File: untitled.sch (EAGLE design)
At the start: 70 parts, among them IC1 SIM900, IC2 ST1S10PHR, IC3 SMF05C, IC5 BQ24072, IC6 SIM68R, X1 ST-SMB-H, X2 ST-SMB-H

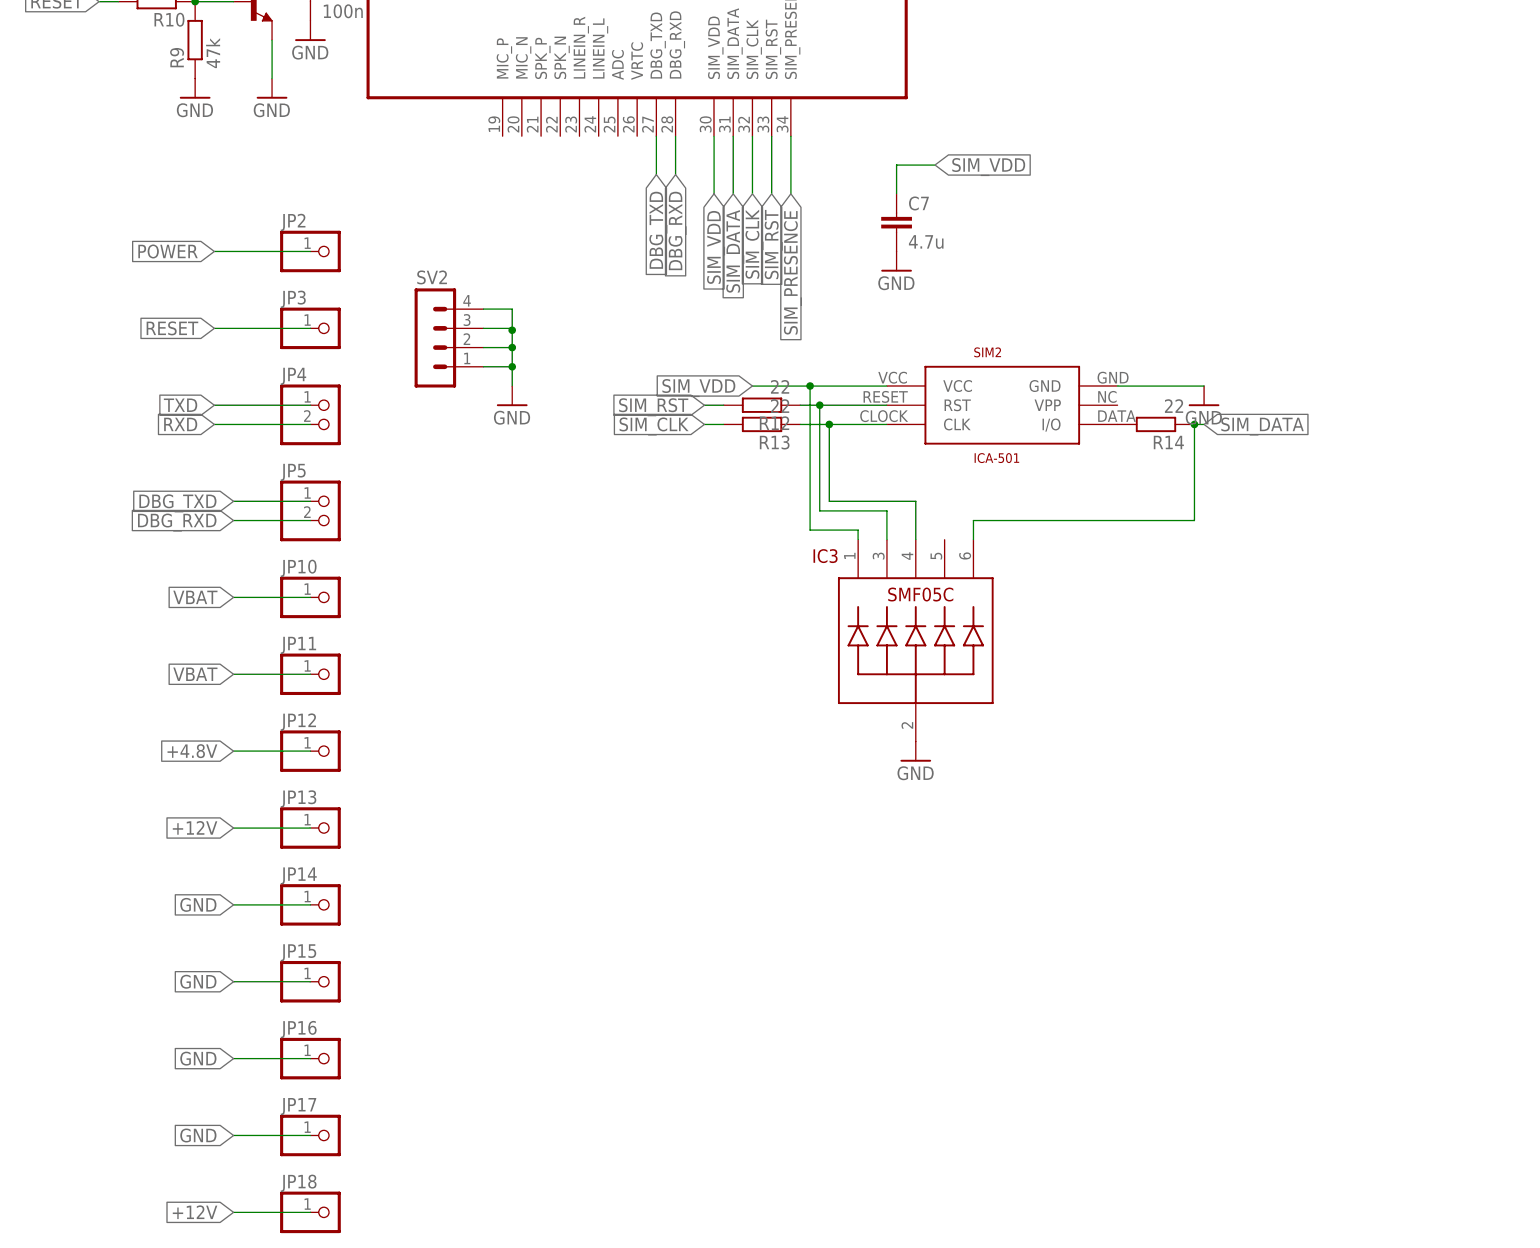
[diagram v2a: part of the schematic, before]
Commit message: SeedStudio preparation
GSM fotprint, polygons, thermals
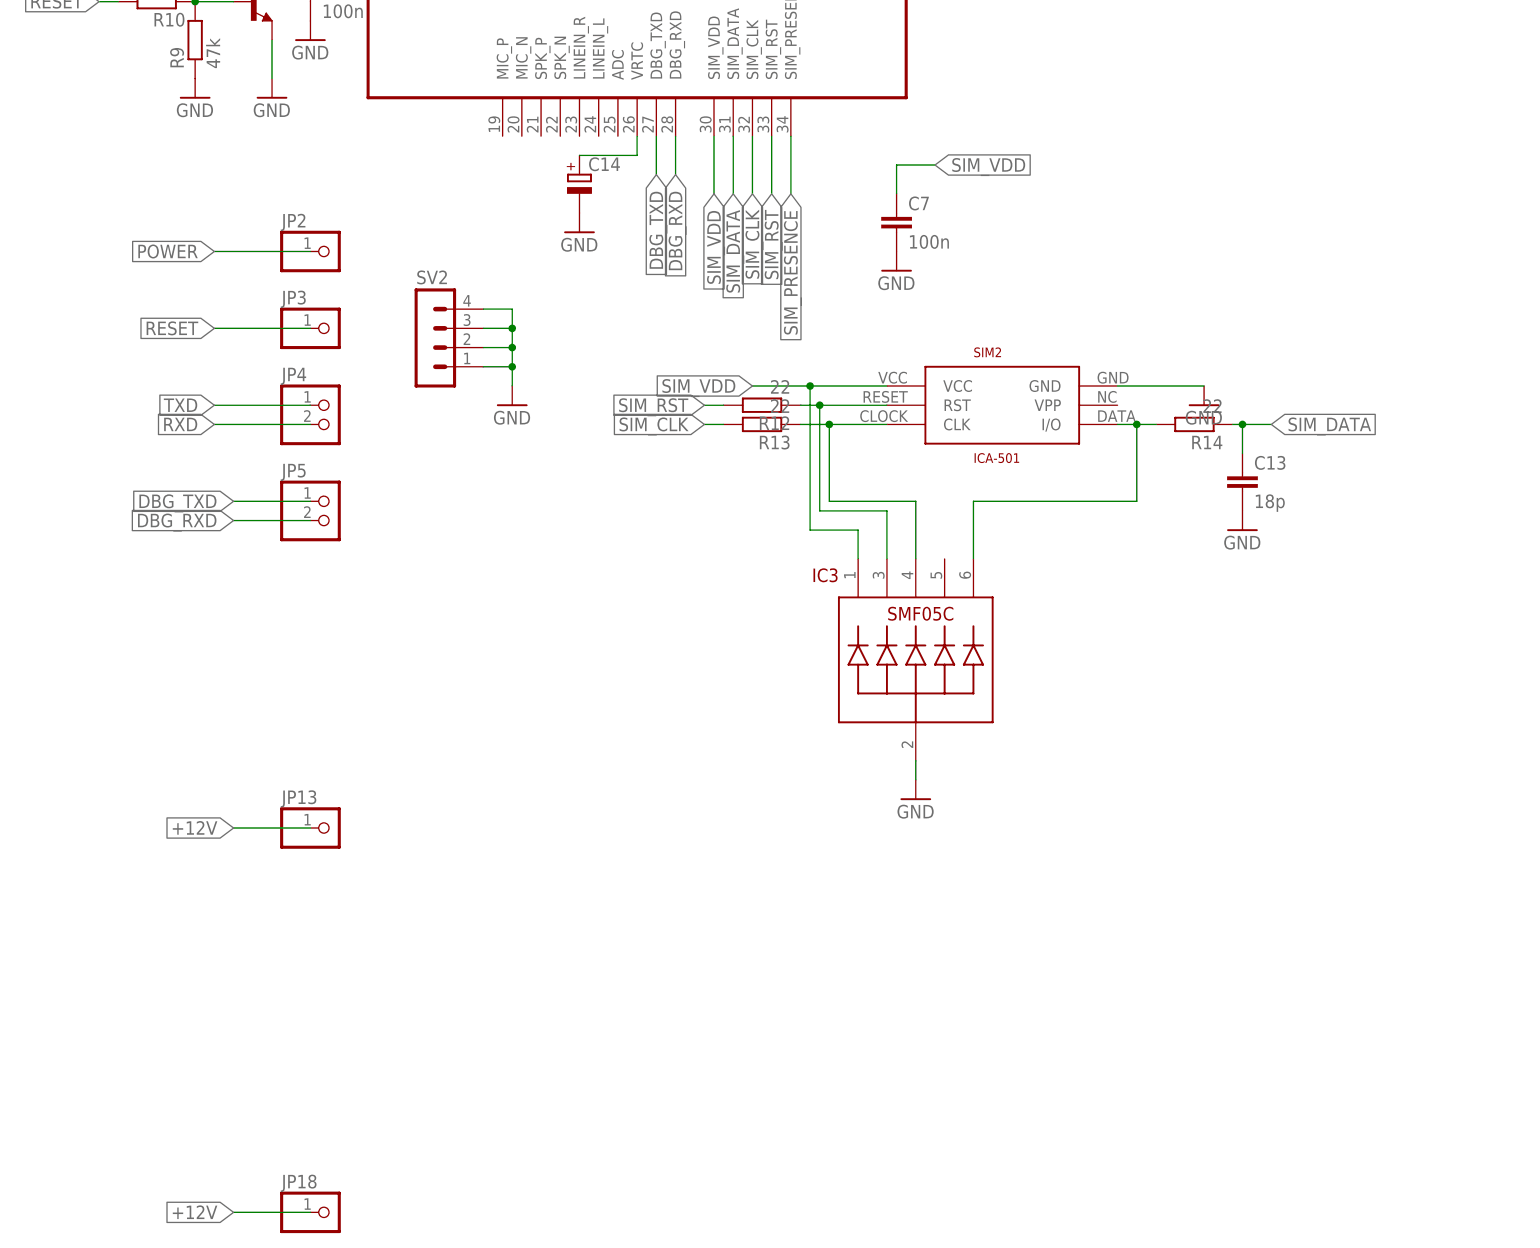
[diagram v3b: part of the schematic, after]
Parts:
- removed JP10, JP11, JP12, JP14, JP15, JP16, JP17: (no value), pinhead:PINHD-1X1
- added C13: 18p, resistor:C-EUC0805
- added C14: (no value), rcl:CPOL-EUA/3216-18R
- C7: value 4.7u -> 100n
- L1: device CDRH6D38:INDUCTOR-SUMIDA-CDRH4D18 -> inductor-sumida-cdrh4d18:INDUCTOR-SUMIDA-CDRH4D18
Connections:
- new net N$15: IC3.6, R14.2, SIM2.I/O
- net +4.8V: no longer JP12.1
- net GND: now also C13.2, C14.-; no longer JP14.1, JP15.1, JP16.1, JP17.1
- net N$17: now also C14.+, IC1G$1.VRTC; no longer R14.2, SIM2.I/O
- net SIM_DATA: now also C13.1; no longer IC3.6
- net VBAT: no longer JP10.1, JP11.1
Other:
- moved on the sheet: IC3, R14

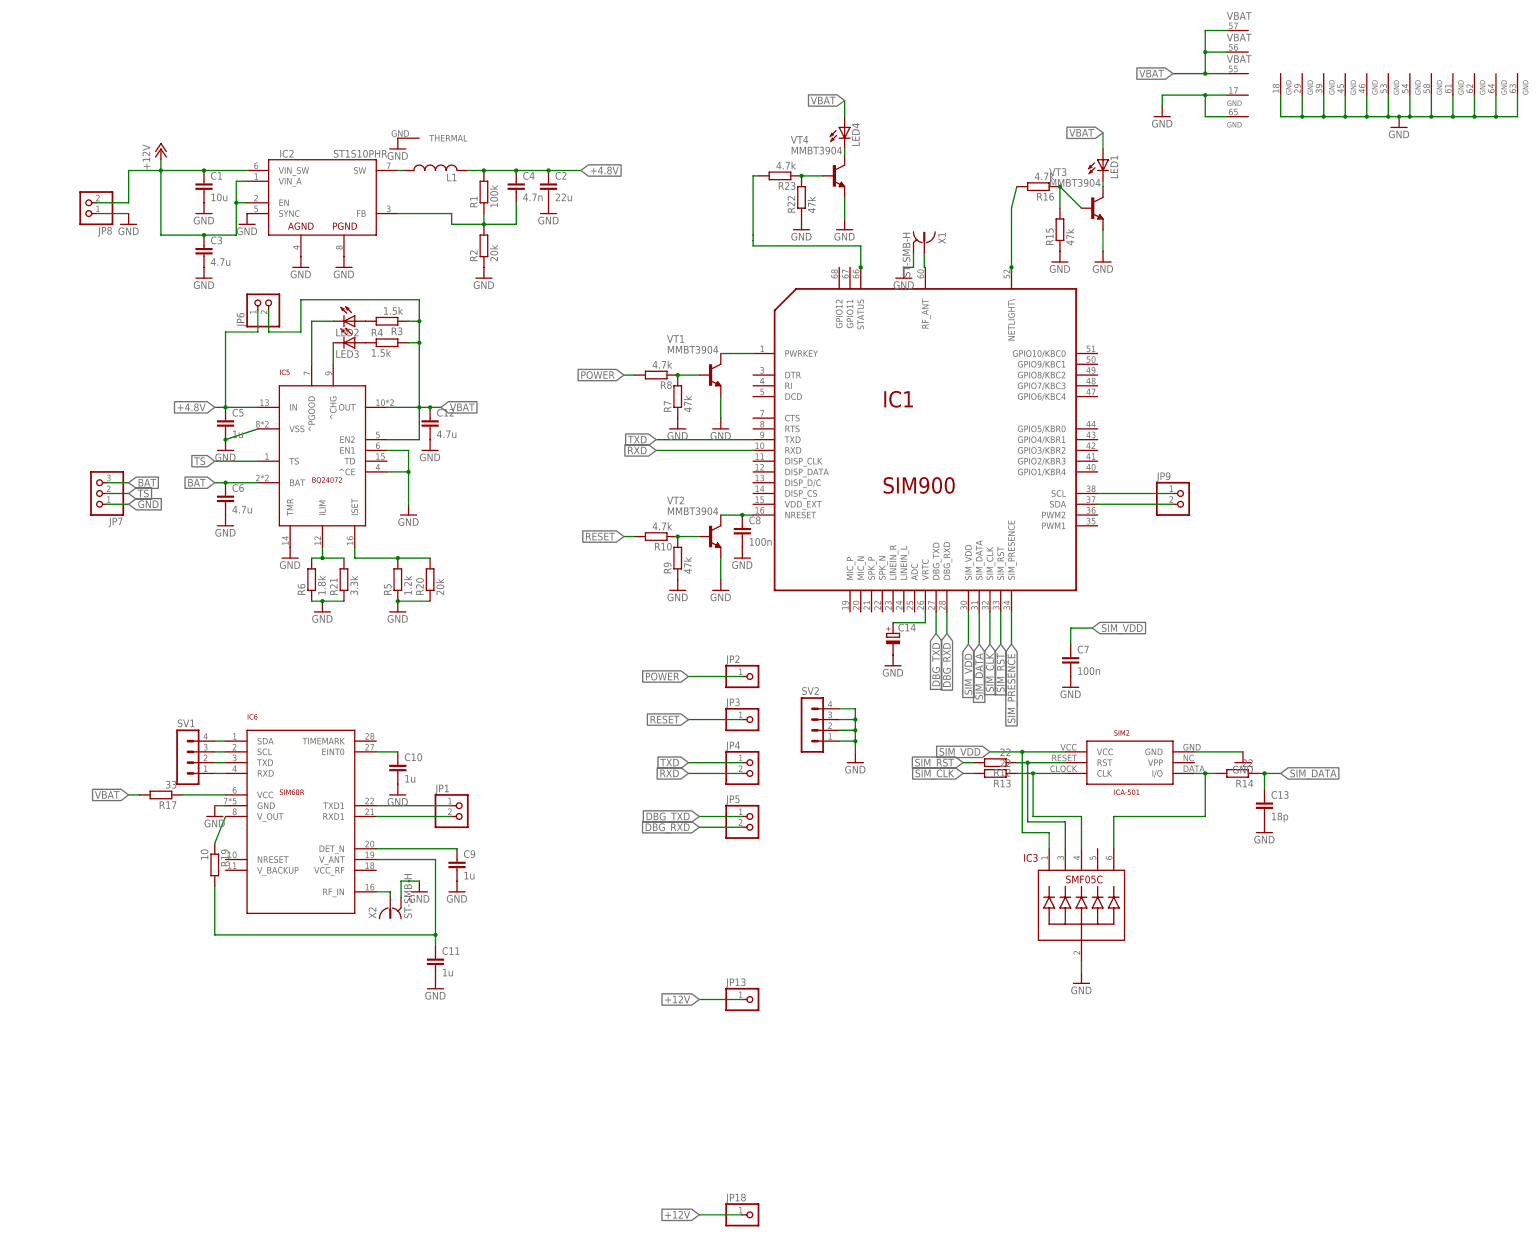
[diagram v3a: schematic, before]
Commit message: BQ now on the top
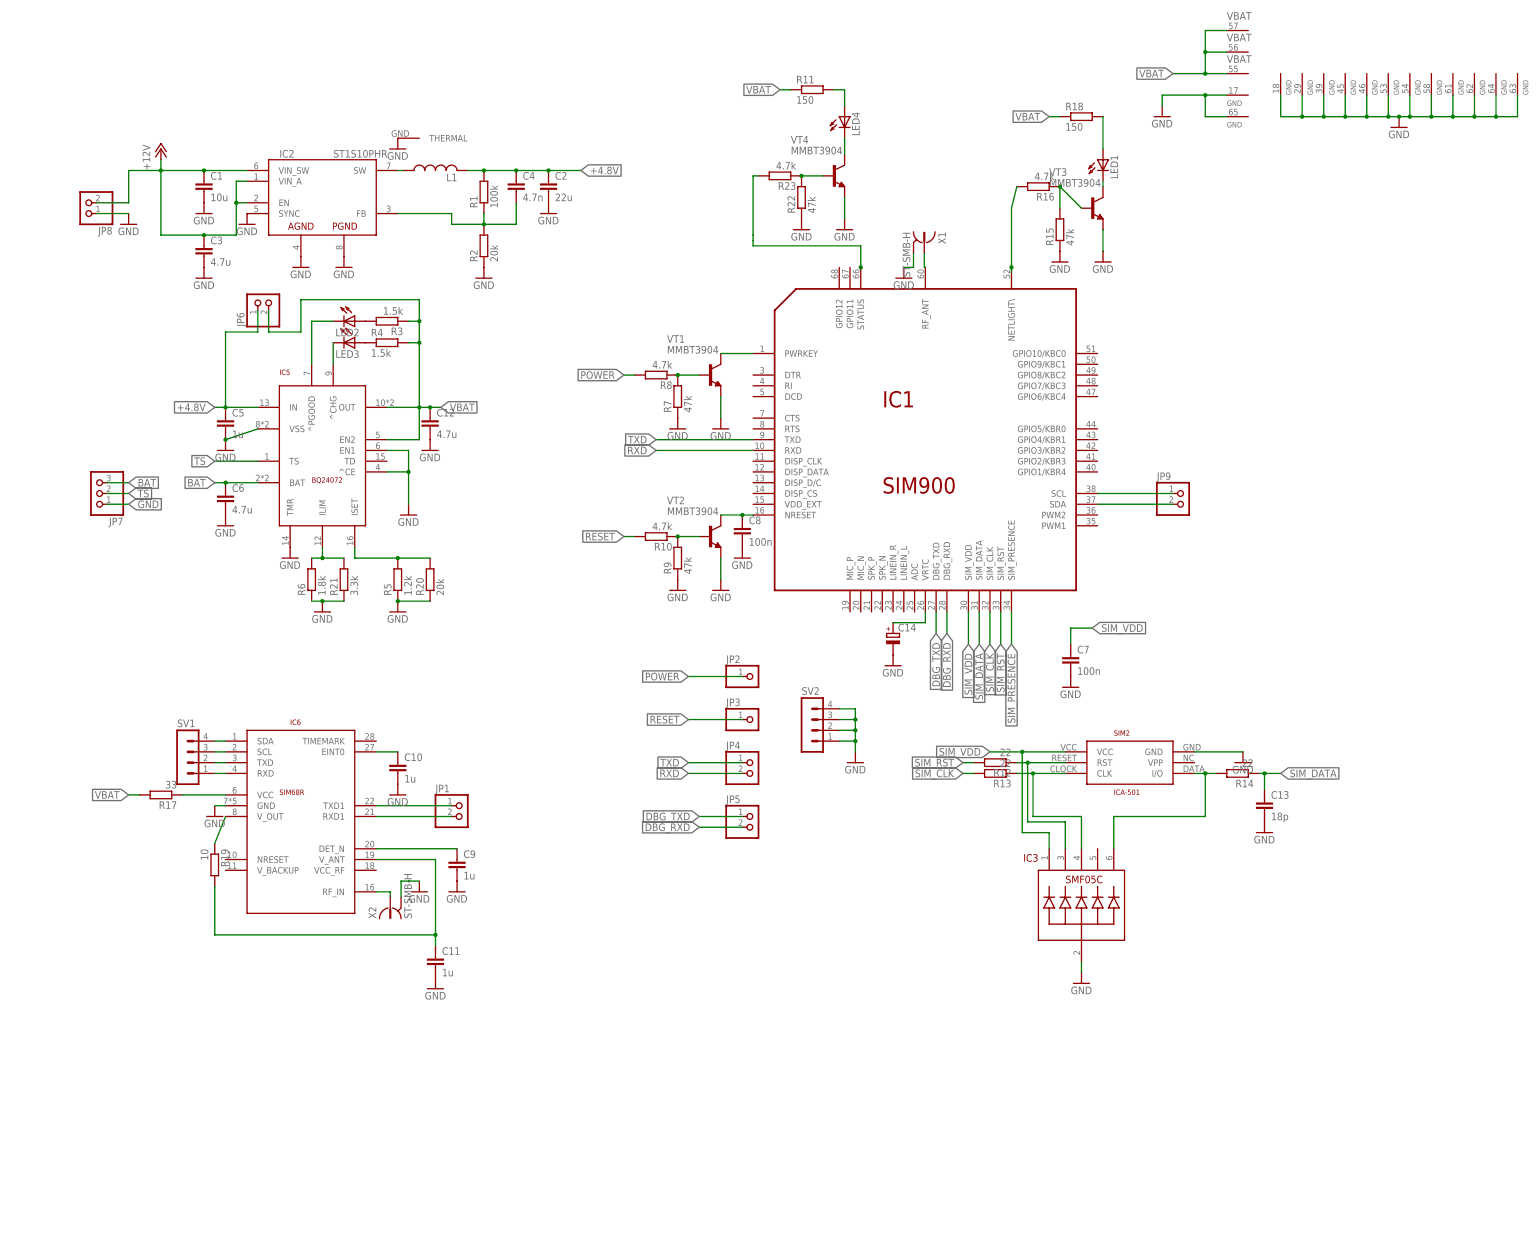
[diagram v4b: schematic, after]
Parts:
- removed JP13, JP18: (no value), pinhead:PINHD-1X1
- added R11, R18: 150, rcl:R-EU_R0805
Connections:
- new net N$36: LED4.A, R11.2
- new net N$45: LED1.A, R18.2
- net +12V: no longer JP13.1, JP18.1
- net VBAT: now also R11.1, R18.1; no longer LED1.A, LED4.A
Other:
- moved on the sheet: LED4
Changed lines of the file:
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@@
 <?xml version="1.0" encoding="utf-8"?>
 <!DOCTYPE eagle SYSTEM "eagle.dtd">
-<eagle version="6.5.0">
+<eagle version="6.4">
 <drawing>
 <settings>
@@
 <setting verticaltext="up"/>
 </settings>
-<grid distance="0.1" unitdist="inch" unit="inch" style="lines" multiple="1" display="no" altdistance="0.01" altunitdist="inch" altunit="inch"/>
+<grid distance="0.05" unitdist="inch" unit="inch" style="lines" multiple="1" display="no" altdistance="0.01" altunitdist="inch" altunit="inch"/>
 <layers>
 <layer number="1" name="Top" color="4" fill="1" visible="no" active="no"/>
@@
 <part name="SIM2" library="ICA-501" deviceset="ICA-501" device=""/>
 <part name="GND27" library="supply1" deviceset="GND" device=""/>
-<part name="JP13" library="pinhead" deviceset="PINHD-1X1" device=""/>
-<part name="JP18" library="pinhead" deviceset="PINHD-1X1" device=""/>
 <part name="C13" library="resistor" deviceset="C-EU" device="C0805" value="18p"/>
 <part name="GND38" library="supply1" deviceset="GND" device=""/>
 <part name="C14" library="rcl" deviceset="CPOL-EU" device="A/3216-18R"/>
 <part name="GND39" library="supply1" deviceset="GND" device=""/>
+<part name="R11" library="rcl" deviceset="R-EU_" device="R0805" value="150"/>
+<part name="R18" library="rcl" deviceset="R-EU_" device="R0805" value="150"/>
 </parts>
 <sheets>
@@
 <instance part="GND36" gate="1" x="-39.37" y="80.01"/>
 <instance part="R23" gate="G$1" x="-44.45" y="92.71" rot="R180"/>
-<instance part="LED4" gate="G$1" x="-29.21" y="101.6"/>
+<instance part="LED4" gate="G$1" x="-29.21" y="104.14"/>
 <instance part="IC6" gate="G$1" x="-157.48" y="-58.42"/>
 <instance part="SV2" gate="1" x="-38.1" y="-35.56"/>
@@
 <instance part="IC2" gate="G$2" x="-134.62" y="101.6" rot="R270"/>
 <instance part="GND27" gate="1" x="-134.62" y="99.06"/>
-<instance part="JP13" gate="G$1" x="-50.8" y="-101.6"/>
-<instance part="JP18" gate="G$1" x="-50.8" y="-152.4"/>
 <instance part="C13" gate="G$1" x="69.85" y="-54.61"/>
 <instance part="GND38" gate="1" x="69.85" y="-62.23"/>
 <instance part="C14" gate="G$1" x="-17.78" y="-15.24"/>
 <instance part="GND39" gate="1" x="-17.78" y="-22.86"/>
+<instance part="R11" gate="G$1" x="-36.83" y="113.03"/>
+<instance part="R18" gate="G$1" x="26.67" y="106.68"/>
 </instances>
 <busses>
@@
 <wire x1="-198.12" y1="93.98" x2="-190.5" y2="93.98" width="0.1524" layer="91"/>
 </segment>
-<segment>
-<pinref part="JP13" gate="G$1" pin="1"/>
-<wire x1="-53.34" y1="-101.6" x2="-63.5" y2="-101.6" width="0.1524" layer="91"/>
-<label x="-63.5" y="-101.6" size="1.778" layer="95" rot="R180" xref="yes"/>
-</segment>
-<segment>
-<pinref part="JP18" gate="G$1" pin="1"/>
-<wire x1="-53.34" y1="-152.4" x2="-63.5" y2="-152.4" width="0.1524" layer="91"/>
-<label x="-63.5" y="-152.4" size="1.778" layer="95" rot="R180" xref="yes"/>
-</segment>
 </net>
 <net name="N$1" class="0">
@@
 </segment>
 <segment>
-<pinref part="LED1" gate="G$1" pin="A"/>
-<wire x1="31.75" y1="99.06" x2="31.75" y2="102.87" width="0.1524" layer="91"/>
-<label x="31.75" y="102.87" size="1.778" layer="95" rot="R180" xref="yes"/>
+<label x="19.05" y="106.68" size="1.778" layer="95" rot="R180" xref="yes"/>
+<pinref part="R18" gate="G$1" pin="1"/>
+<wire x1="21.59" y1="106.68" x2="19.05" y2="106.68" width="0.1524" layer="91"/>
 </segment>
 <segment>
@@
 </segment>
 <segment>
-<pinref part="LED4" gate="G$1" pin="A"/>
-<wire x1="-29.21" y1="106.68" x2="-29.21" y2="110.49" width="0.1524" layer="91"/>
-<label x="-29.21" y="110.49" size="1.778" layer="95" rot="R180" xref="yes"/>
+<pinref part="R11" gate="G$1" pin="1"/>
+<wire x1="-41.91" y1="113.03" x2="-44.45" y2="113.03" width="0.1524" layer="91"/>
+<label x="-44.45" y="113.03" size="1.778" layer="95" rot="R180" xref="yes"/>
 </segment>
 </net>
@@
 <pinref part="VT4" gate="G$1" pin="C"/>
 <pinref part="LED4" gate="G$1" pin="C"/>
-<wire x1="-29.21" y1="97.79" x2="-29.21" y2="99.06" width="0.1524" layer="91"/>
+<wire x1="-29.21" y1="97.79" x2="-29.21" y2="101.6" width="0.1524" layer="91"/>
 </segment>
 </net>
@@
 </segment>
 </net>
+<net name="N$36" class="0">
+<segment>
+<pinref part="R11" gate="G$1" pin="2"/>
+<pinref part="LED4" gate="G$1" pin="A"/>
+<wire x1="-31.75" y1="113.03" x2="-29.21" y2="113.03" width="0.1524" layer="91"/>
+<wire x1="-29.21" y1="113.03" x2="-29.21" y2="109.22" width="0.1524" layer="91"/>
+</segment>
+</net>
+<net name="N$45" class="0">
+<segment>
+<pinref part="R18" gate="G$1" pin="2"/>
+<pinref part="LED1" gate="G$1" pin="A"/>
+<wire x1="31.75" y1="106.68" x2="31.75" y2="99.06" width="0.1524" layer="91"/>
+</segment>
+</net>
